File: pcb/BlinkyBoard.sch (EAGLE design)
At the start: 25 parts, among them Q1 16 MHz

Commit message: Add series resistor to the output data line, so it can be removed from the flex strip
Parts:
- added R3: ??, blinkiverse:R_US
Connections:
- new net LED_DATA: R3.2, U$9.DATA
- net D13: now also R3.1; no longer U$9.DATA
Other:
- note added: "BlinkyTape LED controller RevH"
- note added: "http://blinkinlabs.com/blinkytape"
- note removed: "BlinkyTape LED controller RevD"
- note removed: "http://blinkiverse.com"
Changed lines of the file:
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@@
 <?xml version="1.0" encoding="utf-8"?>
 <!DOCTYPE eagle SYSTEM "eagle.dtd">
-<eagle version="6.4">
+<eagle version="6.5.0">
 <drawing>
 <settings>
@@
 <part name="GND9" library="supply1" deviceset="GND" device=""/>
 <part name="U$9" library="blinkiverse" deviceset="WS2812B_CONNECTOR" device=""/>
+<part name="R3" library="blinkiverse" deviceset="R_US" device="" value="??"/>
 </parts>
 <sheets>
 <sheet>
 <plain>
-<text x="104.14" y="-30.48" size="2.54" layer="94">BlinkyTape LED controller RevD</text>
-<text x="104.14" y="-35.56" size="2.54" layer="94">http://blinkiverse.com</text>
+<text x="104.14" y="-30.48" size="2.54" layer="94">BlinkyTape LED controller RevH</text>
+<text x="104.14" y="-35.56" size="2.54" layer="94">http://blinkinlabs.com/blinkytape</text>
 <text x="177.8" y="-30.48" size="2.54" layer="94">CC 2.5 BY-SA</text>
 <text x="190.5" y="-53.34" size="2.54" layer="94">1</text>
@@
 <instance part="GND9" gate="1" x="20.32" y="63.5"/>
 <instance part="U$9" gate="G$1" x="172.72" y="33.02"/>
+<instance part="R3" gate="G$1" x="152.4" y="33.02"/>
 </instances>
 <busses>
@@
 </segment>
 </net>
-<net name="D13" class="0">
-<segment>
-<pinref part="U$2" gate="G$1" pin="(ICP3/CLK0/OC4A)PC7"/>
-<wire x1="96.52" y1="60.96" x2="99.06" y2="60.96" width="0.1524" layer="91"/>
-<label x="99.06" y="60.96" size="1.778" layer="95" xref="yes"/>
-</segment>
+<net name="LED_DATA" class="0">
 <segment>
 <wire x1="167.64" y1="33.02" x2="157.48" y2="33.02" width="0.1524" layer="91"/>
-<label x="157.48" y="33.02" size="1.778" layer="95" rot="R180" xref="yes"/>
 <pinref part="U$9" gate="G$1" pin="DATA"/>
+<pinref part="R3" gate="G$1" pin="2"/>
 </segment>
 </net>
@@
 </segment>
 </net>
+<net name="D13" class="0">
+<segment>
+<pinref part="U$2" gate="G$1" pin="(ICP3/CLK0/OC4A)PC7"/>
+<wire x1="96.52" y1="60.96" x2="99.06" y2="60.96" width="0.1524" layer="91"/>
+<label x="99.06" y="60.96" size="1.778" layer="95" xref="yes"/>
+</segment>
+<segment>
+<pinref part="R3" gate="G$1" pin="1"/>
+<wire x1="147.32" y1="33.02" x2="144.78" y2="33.02" width="0.1524" layer="91"/>
+<label x="144.78" y="33.02" size="1.778" layer="95" rot="R180" xref="yes"/>
+</segment>
+</net>

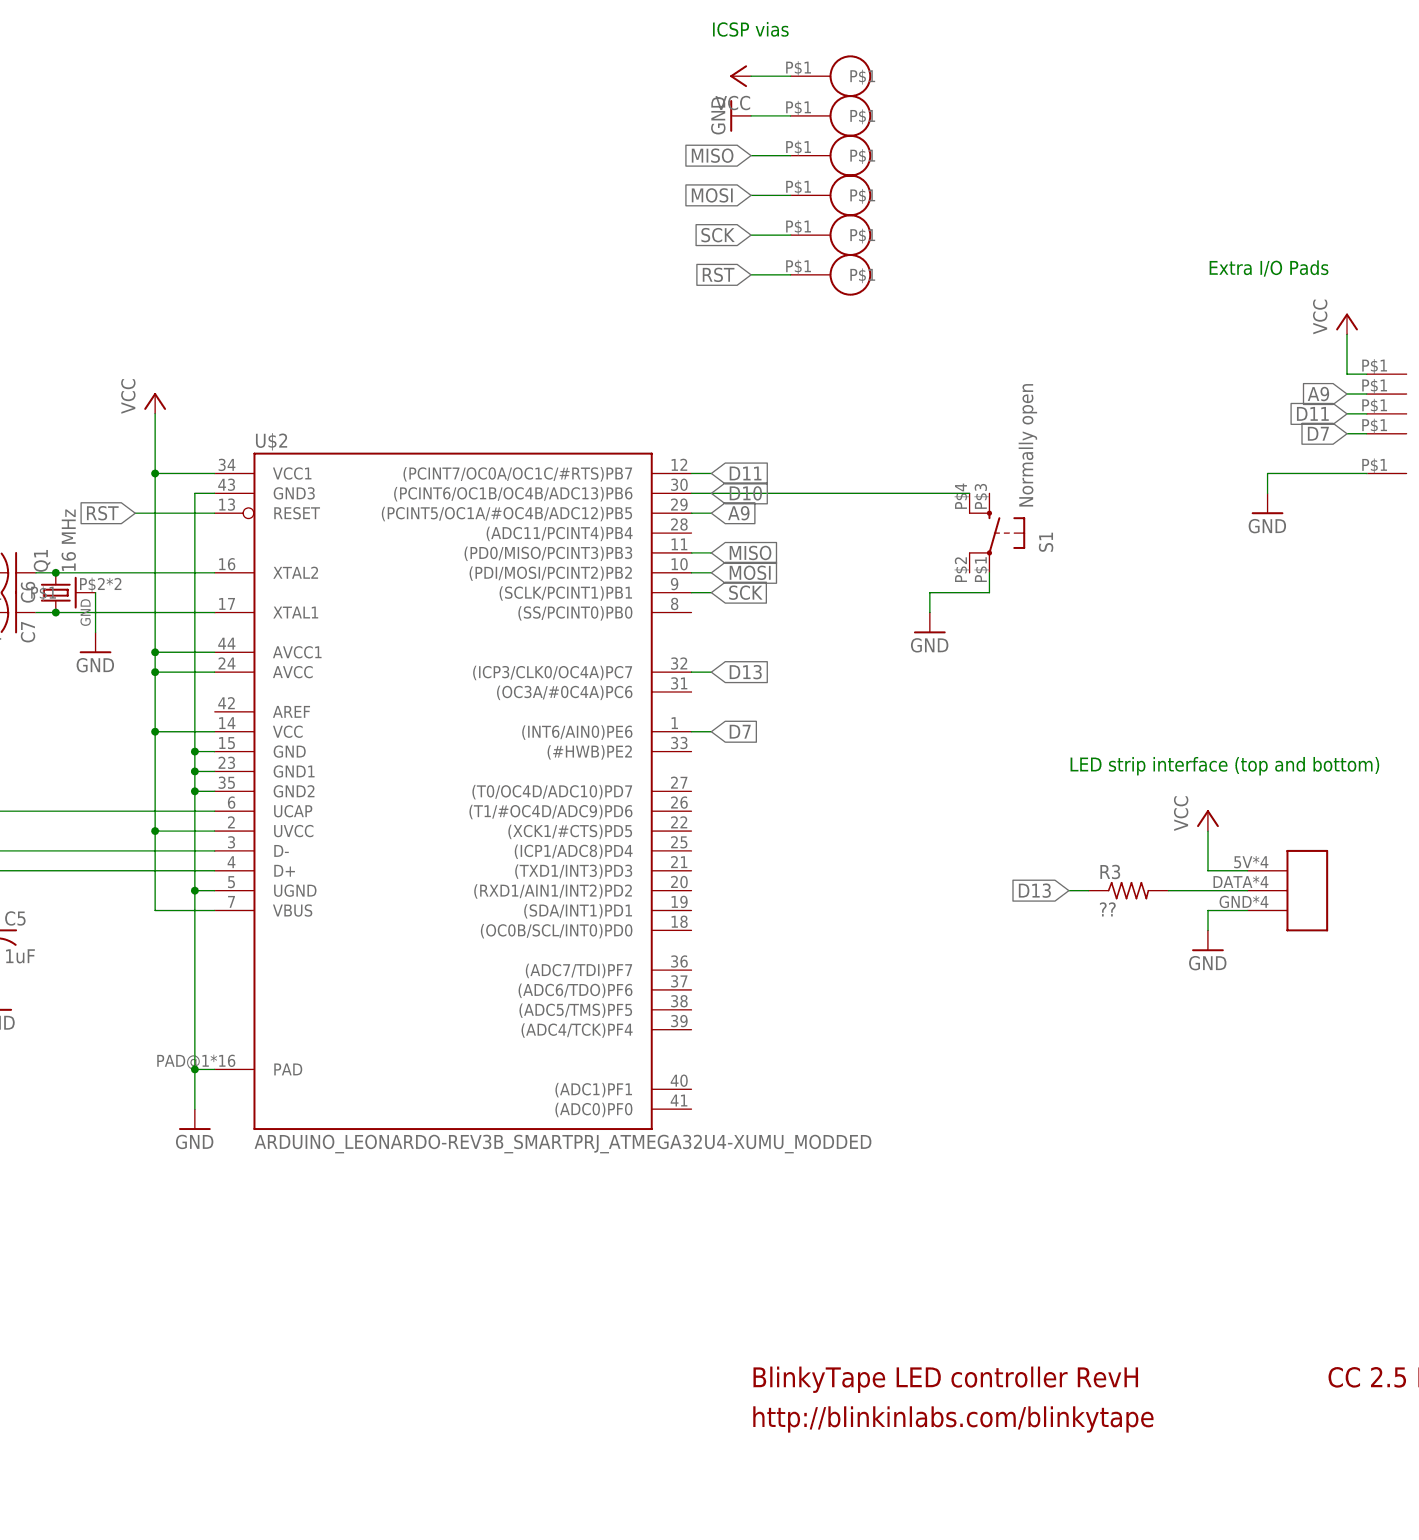
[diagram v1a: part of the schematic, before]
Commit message: RevI PCB, improved component spacing and power routing
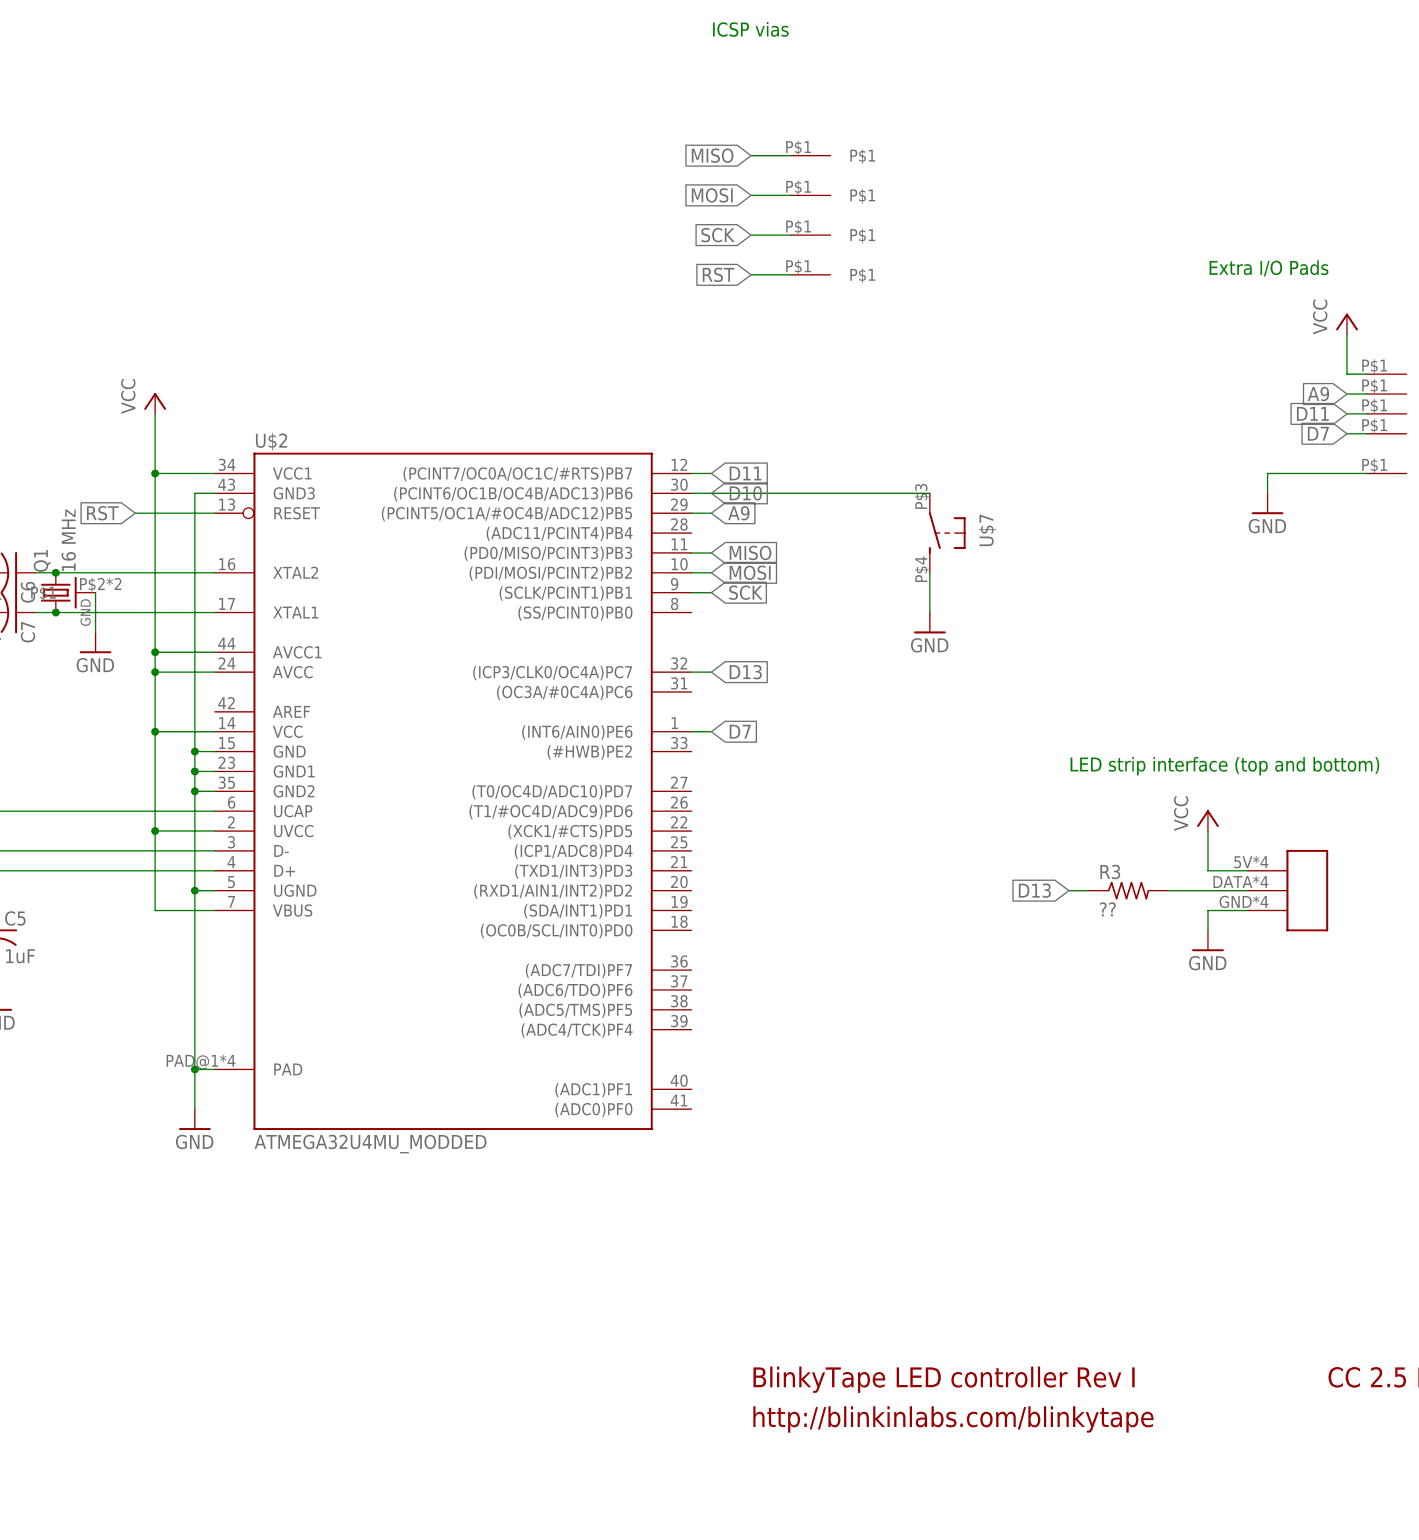
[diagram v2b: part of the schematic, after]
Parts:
- removed S1: Normally open, blinkiverse:GLOWBOARD_KMR211G
- removed U$8: TEST_VIA, blinkiverse:TEST_VIA
- Q1: device blinkiverse:CRYSTAL_4PAD2520 -> blinkinlabs:CRYSTAL_4PAD2520
- U$1, U$3, U$5, U$6: value TEST_VIA -> TEST_PAD_SMT; device blinkiverse:TEST_VIA -> blinkinlabs:TEST_PAD_SMT
- U$2: value ARDUINO_LEONARDO-REV3B_SMARTPRJ_ATMEGA32U4-XUMU_MODDED -> ATMEGA32U4MU_MODDED; device blinkiverse:ARDUINO_LEONARDO-REV3B_SMARTPRJ_ATMEGA32U4-XUMU_MODDED -> blinkinlabs:ATMEGA32U4MU_MODDED
- U$4: value MICRO_USBSMT+THRUHULE -> USB_MICROSMT+THRUHULE; device blinkiverse:MICRO_USBSMT+THRUHULE -> blinkinlabs:USB_MICROSMT+THRUHULE
- U$7: value TEST_VIA -> (none); device blinkiverse:TEST_VIA -> blinkinlabs:BUTTON_MOMENTARY
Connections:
- net D10: now also U$7.P; no longer S1.S1
- net GND: now also U$7.S; no longer S1.P, U$7.P$1
- net VCC: no longer U$8.P$1
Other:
- note added: "BlinkyTape LED controller Rev I"
- note removed: "BlinkyTape LED controller RevH"
- moved on the sheet: U$2
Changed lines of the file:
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@@
 <?xml version="1.0" encoding="utf-8"?>
 <!DOCTYPE eagle SYSTEM "eagle.dtd">
-<eagle version="6.5.0">
+<eagle version="7.2.0">
 <drawing>
 <settings>
@@
 <layer number="54" name="bGND_GNDA" color="1" fill="9" visible="no" active="no"/>
 <layer number="56" name="wert" color="7" fill="1" visible="no" active="no"/>
+<layer number="57" name="tCAD" color="7" fill="1" visible="no" active="no"/>
+<layer number="90" name="Modules" color="5" fill="1" visible="yes" active="yes"/>
 <layer number="91" name="Nets" color="2" fill="1" visible="yes" active="yes"/>
 <layer number="92" name="Busses" color="1" fill="1" visible="yes" active="yes"/>
@@
 <layer number="97" name="Info" color="7" fill="1" visible="yes" active="yes"/>
 <layer number="98" name="Guide" color="6" fill="1" visible="yes" active="yes"/>
+<layer number="99" name="SpiceOrder" color="7" fill="1" visible="no" active="no"/>
 <layer number="100" name="Muster" color="7" fill="1" visible="no" active="no"/>
 <layer number="101" name="Patch_Top" color="12" fill="4" visible="yes" active="yes"/>
@@
 <layer number="111" name="LPC17xx" color="7" fill="1" visible="yes" active="yes"/>
 <layer number="112" name="tSilk" color="7" fill="1" visible="yes" active="yes"/>
+<layer number="113" name="ReferenceLS" color="7" fill="1" visible="no" active="no"/>
 <layer number="116" name="Patch_BOT" color="9" fill="4" visible="yes" active="yes"/>
+<layer number="118" name="Rect_Pads" color="7" fill="1" visible="no" active="no"/>
 <layer number="121" name="_tsilk" color="7" fill="1" visible="yes" active="yes"/>
 <layer number="122" name="_bsilk" color="7" fill="1" visible="yes" active="yes"/>
@@
 <layer number="132" name="bAdjust" color="7" fill="1" visible="no" active="yes"/>
 <layer number="144" name="Drill_legend" color="7" fill="1" visible="yes" active="yes"/>
+<layer number="150" name="Notes" color="7" fill="1" visible="yes" active="yes"/>
 <layer number="151" name="HeatSink" color="7" fill="1" visible="yes" active="yes"/>
 <layer number="152" name="_bDocu" color="7" fill="1" visible="yes" active="yes"/>
+<layer number="153" name="FabDoc1" color="7" fill="1" visible="yes" active="yes"/>
+<layer number="154" name="FabDoc2" color="7" fill="1" visible="yes" active="yes"/>
+<layer number="155" name="FabDoc3" color="7" fill="1" visible="yes" active="yes"/>
 <layer number="199" name="Contour" color="7" fill="1" visible="yes" active="yes"/>
 <layer number="200" name="200bmp" color="1" fill="10" visible="no" active="no"/>
@@
 <layer number="223" name="223bmp" color="7" fill="1" visible="yes" active="yes"/>
 <layer number="224" name="224bmp" color="7" fill="1" visible="yes" active="yes"/>
+<layer number="231" name="Eagle3D_PG1" color="7" fill="1" visible="no" active="no"/>
+<layer number="232" name="Eagle3D_PG2" color="7" fill="1" visible="no" active="no"/>
+<layer number="233" name="Eagle3D_PG3" color="7" fill="1" visible="no" active="no"/>
 <layer number="248" name="Housing" color="7" fill="1" visible="yes" active="yes"/>
 <layer number="249" name="Edge" color="7" fill="1" visible="yes" active="yes"/>
@@
 <layer number="251" name="SMDround" color="7" fill="1" visible="no" active="no"/>
 <layer number="254" name="cooling" color="7" fill="1" visible="yes" active="yes"/>
+<layer number="255" name="routoute" color="7" fill="1" visible="yes" active="yes"/>
 </layers>
-<schematic>
+<schematic xreflabel="%F%N/%S.%C%R" xrefpart="/%S.%C%R">
 <attributes>
 </attributes>
@@
 </variantdefs>
 <classes>
-<class number="0" name="default" width="0" drill="0">
+<class number="0" name="data" width="0.2" drill="0.3">
+<clearance class="0" value="0.2"/>
+</class>
+<class number="1" name="power" width="0.24" drill="0.3">
+<clearance class="1" value="0.2"/>
 </class>
 </classes>
@@
 <part name="P+1" library="supply1" deviceset="VCC" device=""/>
 <part name="FRAME1" library="frames" deviceset="FRAME_A_L" device=""/>
-<part name="U$2" library="blinkiverse" deviceset="ARDUINO_LEONARDO-REV3B_SMARTPRJ_ATMEGA32U4-XU" device="MU_MODDED" value="ARDUINO_LEONARDO-REV3B_SMARTPRJ_ATMEGA32U4-XUMU_MODDED"/>
+<part name="U$2" library="blinkinlabs" deviceset="ATMEGA32U4" device="MU_MODDED" value="ATMEGA32U4MU_MODDED"/>
 <part name="GND8" library="supply1" deviceset="GND" device=""/>
 <part name="P+6" library="supply1" deviceset="VCC" device=""/>
 <part name="P+7" library="supply1" deviceset="VCC" device=""/>
-<part name="S1" library="blinkiverse" deviceset="GLOWBOARD_KMR211G" device="" value="Normally open"/>
-<part name="Q1" library="blinkiverse" deviceset="CRYSTAL_4PAD" device="2520" value="16 MHz"/>
+<part name="Q1" library="blinkinlabs" deviceset="CRYSTAL_4PAD" device="2520" value="16 MHz"/>
 <part name="C4" library="blinkiverse" deviceset="C_US" device="" value="0.1uF"/>
 <part name="P+3" library="supply1" deviceset="VCC" device=""/>
 <part name="GND4" library="supply1" deviceset="GND" device=""/>
 <part name="P+4" library="supply1" deviceset="VCC" device=""/>
-<part name="U$4" library="blinkiverse" deviceset="MICRO_USB" device="SMT+THRUHULE"/>
+<part name="U$4" library="blinkinlabs" deviceset="USB_MICRO" device="SMT+THRUHULE"/>
 <part name="GND5" library="supply1" deviceset="GND" device=""/>
-<part name="U$1" library="blinkiverse" deviceset="TEST_VIA" device=""/>
-<part name="U$3" library="blinkiverse" deviceset="TEST_VIA" device=""/>
-<part name="U$5" library="blinkiverse" deviceset="TEST_VIA" device=""/>
-<part name="U$6" library="blinkiverse" deviceset="TEST_VIA" device=""/>
-<part name="U$7" library="blinkiverse" deviceset="TEST_VIA" device=""/>
-<part name="U$8" library="blinkiverse" deviceset="TEST_VIA" device=""/>
-<part name="P+2" library="supply1" deviceset="VCC" device=""/>
-<part name="GND1" library="supply1" deviceset="GND" device=""/>
+<part name="U$1" library="blinkinlabs" deviceset="TEST_PAD_SMT" device=""/>
+<part name="U$3" library="blinkinlabs" deviceset="TEST_PAD_SMT" device=""/>
+<part name="U$5" library="blinkinlabs" deviceset="TEST_PAD_SMT" device=""/>
+<part name="U$6" library="blinkinlabs" deviceset="TEST_PAD_SMT" device=""/>
 <part name="GND2" library="supply1" deviceset="GND" device=""/>
 <part name="P+5" library="supply1" deviceset="VCC" device=""/>
@@
 <part name="U$9" library="blinkiverse" deviceset="WS2812B_CONNECTOR" device=""/>
 <part name="R3" library="blinkiverse" deviceset="R_US" device="" value="??"/>
+<part name="U$7" library="blinkinlabs" deviceset="BUTTON_MOMENTARY" device=""/>
 </parts>
 <sheets>
 <sheet>
 <plain>
-<text x="104.14" y="-30.48" size="2.54" layer="94">BlinkyTape LED controller RevH</text>
+<text x="104.14" y="-30.48" size="2.54" layer="94">BlinkyTape LED controller Rev I</text>
 <text x="104.14" y="-35.56" size="2.54" layer="94">http://blinkinlabs.com/blinkytape</text>
 <text x="177.8" y="-30.48" size="2.54" layer="94">CC 2.5 BY-SA</text>
@@
 <instance part="P+6" gate="VCC" x="27.94" y="96.52"/>
 <instance part="P+7" gate="VCC" x="-30.48" y="132.08"/>
-<instance part="S1" gate="1" x="134.62" y="78.74" rot="MR0"/>
 <instance part="Q1" gate="G$1" x="15.24" y="71.12" rot="R90"/>
 <instance part="C4" gate="G$1" x="-20.32" y="121.92"/>
@@
 <instance part="U$5" gate="G$1" x="114.3" y="116.84"/>
 <instance part="U$6" gate="G$1" x="114.3" y="111.76"/>
-<instance part="U$7" gate="G$1" x="114.3" y="132.08"/>
-<instance part="U$8" gate="G$1" x="114.3" y="137.16"/>
-<instance part="P+2" gate="VCC" x="101.6" y="137.16" rot="R90"/>
-<instance part="GND1" gate="1" x="101.6" y="132.08" rot="R270"/>
 <instance part="GND2" gate="1" x="170.18" y="81.28"/>
 <instance part="P+5" gate="VCC" x="180.34" y="106.68"/>
@@
 <instance part="U$9" gate="G$1" x="172.72" y="33.02"/>
 <instance part="R3" gate="G$1" x="152.4" y="33.02"/>
+<instance part="U$7" gate="G$1" x="127" y="78.74" rot="R180"/>
 </instances>
 <busses>
 </busses>
 <nets>
-<net name="GND" class="0">
+<net name="GND" class="1">
 <segment>
 <pinref part="C5" gate="G$1" pin="2"/>
@@
 </segment>
 <segment>
-<wire x1="127" y1="68.58" x2="127" y2="71.12" width="0.1524" layer="91"/>
+<wire x1="127" y1="68.58" x2="127" y2="73.66" width="0.1524" layer="91"/>
 <pinref part="GND7" gate="1" pin="GND"/>
-<pinref part="S1" gate="1" pin="P"/>
-<wire x1="134.62" y1="73.66" x2="134.62" y2="71.12" width="0.1524" layer="91"/>
-<wire x1="134.62" y1="71.12" x2="127" y2="71.12" width="0.1524" layer="91"/>
+<pinref part="U$7" gate="G$1" pin="S"/>
 </segment>
 <segment>
@@
 </segment>
 <segment>
-<pinref part="GND1" gate="1" pin="GND"/>
-<pinref part="U$7" gate="G$1" pin="P$1"/>
-<wire x1="104.14" y1="132.08" x2="109.22" y2="132.08" width="0.1524" layer="91"/>
-</segment>
-<segment>
 <pinref part="GND2" gate="1" pin="GND"/>
 <wire x1="182.88" y1="86.36" x2="170.18" y2="86.36" width="0.1524" layer="91"/>
@@
 <net name="D10" class="0">
 <segment>
-<pinref part="S1" gate="1" pin="S1"/>
 <pinref part="U$2" gate="G$1" pin="(PCINT6/OC1B/OC4B/ADC13)PB6"/>
-<wire x1="96.52" y1="83.82" x2="132.08" y2="83.82" width="0.1524" layer="91"/>
+<wire x1="96.52" y1="83.82" x2="127" y2="83.82" width="0.1524" layer="91"/>
 <label x="99.06" y="83.82" size="1.778" layer="95" xref="yes"/>
+<pinref part="U$7" gate="G$1" pin="P"/>
 </segment>
 </net>
@@
 </segment>
 </net>
-<net name="VCC" class="0">
+<net name="VCC" class="1">
 <segment>
 <wire x1="182.88" y1="99.06" x2="180.34" y2="99.06" width="0.1524" layer="91"/>
@@
 <wire x1="-20.32" y1="71.12" x2="-20.32" y2="40.64" width="0.1524" layer="91"/>
 </segment>
-<segment>
-<pinref part="U$8" gate="G$1" pin="P$1"/>
-<pinref part="P+2" gate="VCC" pin="VCC"/>
-<wire x1="109.22" y1="137.16" x2="104.14" y2="137.16" width="0.1524" layer="91"/>
-</segment>
-</net>
+</net>
